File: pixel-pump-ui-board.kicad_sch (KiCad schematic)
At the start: 40 parts, among them J1 SM10B-SRSS-TB, SW1 B3U-1000P, SW2 B3U-1000P, SW3 B3U-1000P, SW4 B3U-1000P, SW5 B3U-1000P, SW6 B3U-1000P, U1 WS2812B-2020, U10 WS2812B-2020, U11 WS2812B-2020, U12 WS2812B-2020, U2 WS2812B-2020, U3 WS2812B-2020, U4 WS2812B-2020, U5 WS2812B-2020, U6 WS2812B-2020, U7 WS2812B-2020, U8 WS2812B-2020, U9 WS2812B-2020

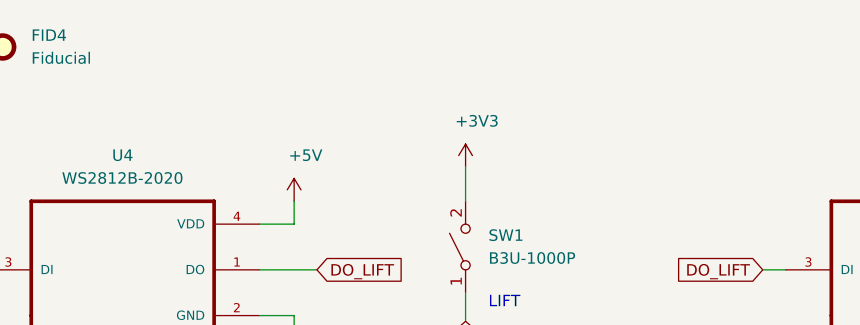
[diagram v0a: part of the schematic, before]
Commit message: Add KiKit Tabs
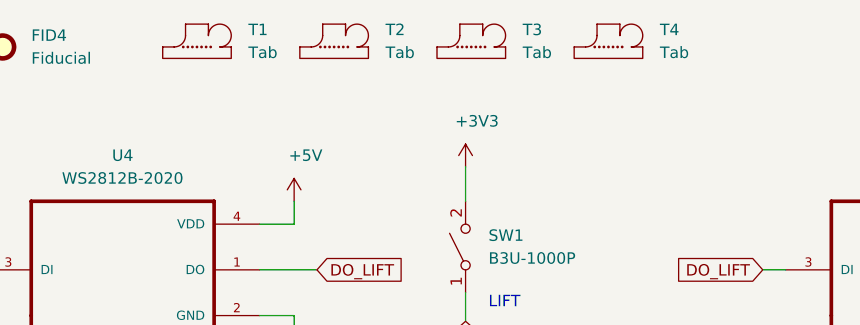
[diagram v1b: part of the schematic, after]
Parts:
- added T1, T2, T3, T4: Tab, kikit:Tab, symbol kikit:Tab
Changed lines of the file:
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@@
     (pin "4")
+  )
+  (symbol (lib_id "kikit:Tab") (at 107.315 18.415 0) (unit 1)
+    (in_bom no) (on_board yes) (fields_autoplaced)
+    (property "Reference" "T2" (id 0) (at 113.03 16.5099 0)
+      (effects (font (size 1.27 1.27)) (justify left))
+    )
+    (property "Value" "Tab" (id 1) (at 113.03 19.0499 0)
+      (effects (font (size 1.27 1.27)) (justify left))
+    )
+    (property "Footprint" "kikit:Tab" (id 2) (at 107.315 18.415 0)
+      (effects (font (size 1.27 1.27)) hide)
+    )
+    (property "Datasheet" "" (id 3) (at 107.315 18.415 0)
+      (effects (font (size 1.27 1.27)) hide)
+    )
   )
   (symbol (lib_id "Connector:TestPoint") (at 166.37 162.56 0) (unit 1)
@@
     (pin "1")
   )
+  (symbol (lib_id "kikit:Tab") (at 137.795 18.415 0) (unit 1)
+    (in_bom no) (on_board yes) (fields_autoplaced)
+    (property "Reference" "T4" (id 0) (at 143.51 16.5099 0)
+      (effects (font (size 1.27 1.27)) (justify left))
+    )
+    (property "Value" "Tab" (id 1) (at 143.51 19.0499 0)
+      (effects (font (size 1.27 1.27)) (justify left))
+    )
+    (property "Footprint" "kikit:Tab" (id 2) (at 137.795 18.415 0)
+      (effects (font (size 1.27 1.27)) hide)
+    )
+    (property "Datasheet" "" (id 3) (at 137.795 18.415 0)
+      (effects (font (size 1.27 1.27)) hide)
+    )
+  )
+  (symbol (lib_id "kikit:Tab") (at 122.555 18.415 0) (unit 1)
+    (in_bom no) (on_board yes) (fields_autoplaced)
+    (property "Reference" "T3" (id 0) (at 128.27 16.5099 0)
+      (effects (font (size 1.27 1.27)) (justify left))
+    )
+    (property "Value" "Tab" (id 1) (at 128.27 19.0499 0)
+      (effects (font (size 1.27 1.27)) (justify left))
+    )
+    (property "Footprint" "kikit:Tab" (id 2) (at 122.555 18.415 0)
+      (effects (font (size 1.27 1.27)) hide)
+    )
+    (property "Datasheet" "" (id 3) (at 122.555 18.415 0)
+      (effects (font (size 1.27 1.27)) hide)
+    )
+  )
   (symbol (lib_id "Device:C") (at 208.28 151.13 0) (unit 1)
     (in_bom yes) (on_board yes) (fields_autoplaced)
@@
     (pin "1")
   )
+  (symbol (lib_id "kikit:Tab") (at 92.075 18.415 0) (unit 1)
+    (in_bom no) (on_board yes) (fields_autoplaced)
+    (property "Reference" "T1" (id 0) (at 97.79 16.5099 0)
+      (effects (font (size 1.27 1.27)) (justify left))
+    )
+    (property "Value" "Tab" (id 1) (at 97.79 19.0499 0)
+      (effects (font (size 1.27 1.27)) (justify left))
+    )
+    (property "Footprint" "kikit:Tab" (id 2) (at 92.075 18.415 0)
+      (effects (font (size 1.27 1.27)) hide)
+    )
+    (property "Datasheet" "" (id 3) (at 92.075 18.415 0)
+      (effects (font (size 1.27 1.27)) hide)
+    )
+  )
   (symbol (lib_id "Connector:TestPoint") (at 139.065 162.56 0) (unit 1)
     (in_bom no) (on_board yes)
@@
       (reference "SW6") (unit 1) (value "B3U-1000P") (footprint "Button_Switch_SMD:SW_SPST_B3U-1000P")
     )
+    (path "/e72e554c-77ed-41d5-a412-fff7c06f9072"
+      (reference "T1") (unit 1) (value "Tab") (footprint "kikit:Tab")
+    )
+    (path "/12afd006-2fae-4dfc-8bcf-24dff936010a"
+      (reference "T2") (unit 1) (value "Tab") (footprint "kikit:Tab")
+    )
+    (path "/71e6c99d-d427-421f-a2a6-5947a80e853a"
+      (reference "T3") (unit 1) (value "Tab") (footprint "kikit:Tab")
+    )
+    (path "/6d2de3ab-9a19-4012-8c9b-7bd04d8cdf7d"
+      (reference "T4") (unit 1) (value "Tab") (footprint "kikit:Tab")
+    )
     (path "/292851f9-6a15-4ba4-8eb1-ea4687cdfd70"

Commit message: Panelize
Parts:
- J1: footprint Connector_JST:JST_SH_SM10B-SRSS-TB_1x10-1MP_P1.00mm_Horizontal -> SM10B-SRSS-TB:SM10B-SRSS-TB
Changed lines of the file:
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@@
     (property "Reference" "J1" (id 0) (at 39.7256 154.94 90))
     (property "Value" "SM10B-SRSS-TB" (id 1) (at 39.7256 157.48 90))
-    (property "Footprint" "Connector_JST:JST_SH_SM10B-SRSS-TB_1x10-1MP_P1.00mm_Horizontal" (id 2) (at 38.1 161.925 0)
+    (property "Footprint" "SM10B-SRSS-TB:SM10B-SRSS-TB" (id 2) (at 38.1 161.925 0)
       (effects (font (size 1.27 1.27)) hide)
     )
@@
     )
     (path "/4370c97a-e5e7-4207-a2ef-180e29cc325d"
-      (reference "J1") (unit 1) (value "SM10B-SRSS-TB") (footprint "Connector_JST:JST_SH_SM10B-SRSS-TB_1x10-1MP_P1.00mm_Horizontal")
+      (reference "J1") (unit 1) (value "SM10B-SRSS-TB") (footprint "SM10B-SRSS-TB:SM10B-SRSS-TB")
     )
     (path "/4a7a146d-e7dd-4c7b-9d76-a5539b538c5b"
